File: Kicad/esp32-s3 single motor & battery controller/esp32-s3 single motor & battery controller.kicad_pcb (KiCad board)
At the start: 4 copper layers, 44.9 x 42 mm, 132 parts, among them J1 JST SH SM04B, J2 7 pin FPC 0.3mm, J3 Conn_01x03, J4 Conn_01x03, J5 Batt Balance connector, Q1 NMOS,12v, Q2 NMOS, 12v, Q3 NMOS,12v,PPak, Q4 NMOS, 12v, Q5 NMOS, 12v, Q7 NMOS,12v,PPak, SW1 SW_Push, SW2 SW_Push, U2 AP63203WU, U3 BQ76905RGRR, U4 BQ24780SRUYR, U5 ESP32-S3, U6 74HC595, Y1 40mhz, 10ppm

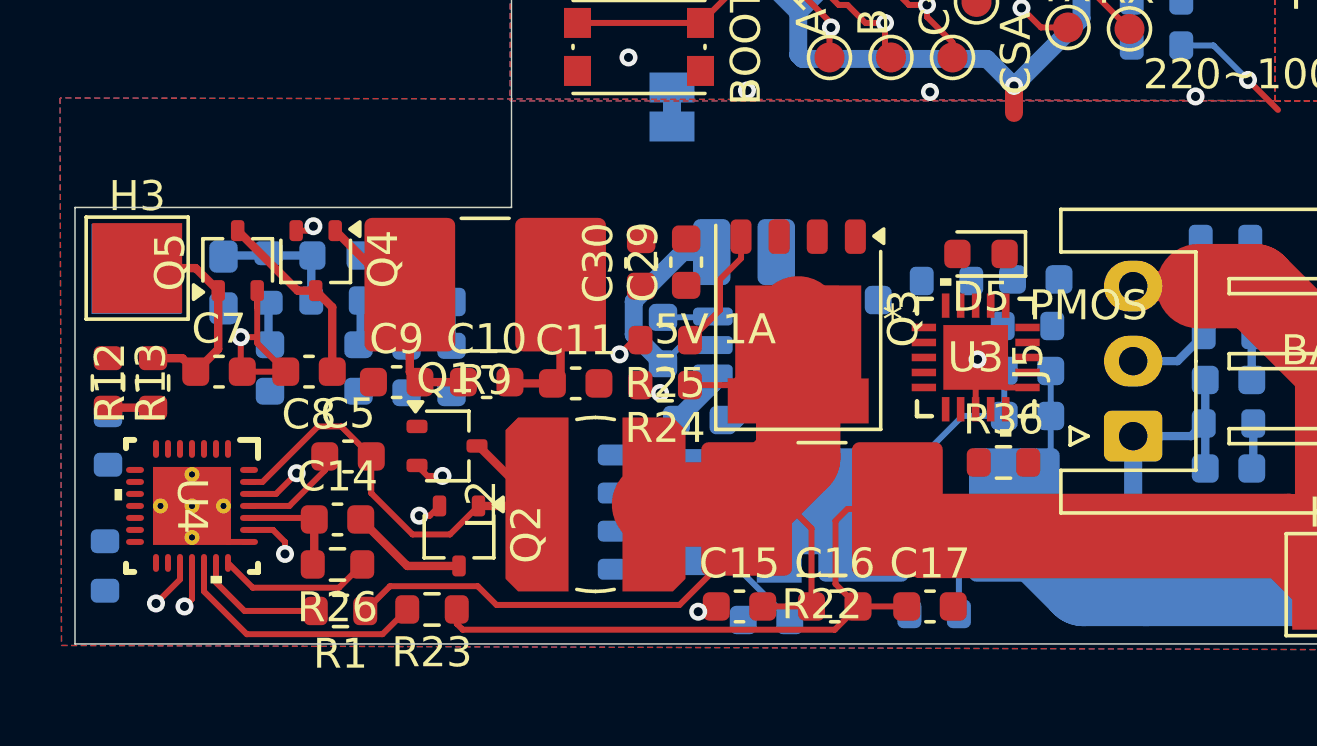
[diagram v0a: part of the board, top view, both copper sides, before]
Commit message: Almost complete charger section, working on balancer
I have a problem with the current sense lines on the balance charger. One loops around with filter capacitors, while the other zigs and zags back and forth on multiple layers! They have to cross each other, and this may lead to a lot of noise.
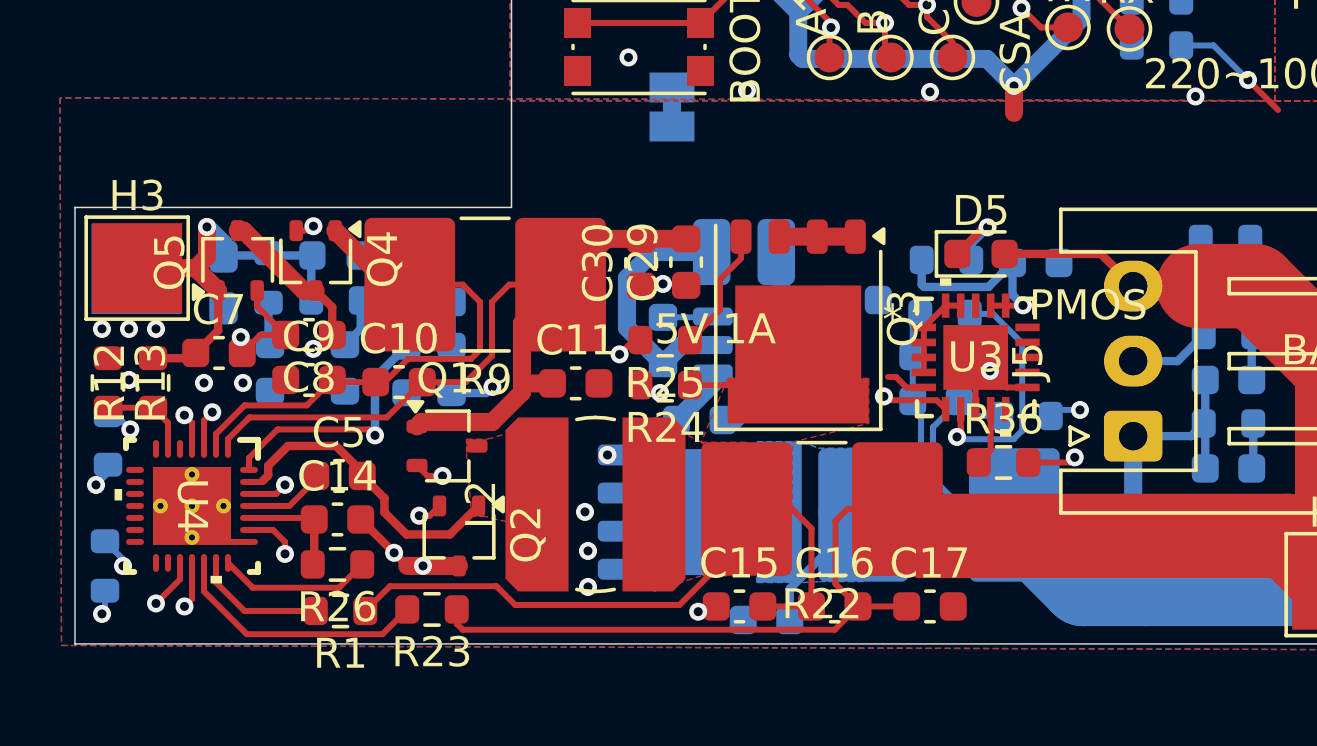
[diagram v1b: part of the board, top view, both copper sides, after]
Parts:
- C11: value 0.01uF -> 0.1uF
- moved R29 7.28 mm to (139.8, 124.4), turned to 180 degrees
- moved C32 3.09 mm to (136.8, 123.9)
- moved C33 3.09 mm to (136.8, 122.4)
- moved C9 2.92 mm to (115.9, 123.2)
- moved C10 2.92 mm to (118.9, 123.3)
- moved R30 2.78 mm to (137.1, 121.0)
- moved C8 1.22 mm to (115.9, 121.7)
- moved C5 0.72 mm to (116.9, 126.4)
- moved R31 0.70 mm to (137.2, 119.2)
- moved C7 0.62 mm to (112.9, 122.3)
- moved C35 0.55 mm to (140.1, 119.3)
- moved C31 0.45 mm to (117.1, 122.8)
- turned D5 to 0 degrees
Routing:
- net /PSU/BATT+: track 59.9 -> 88.8 mm, vias 0 -> 1
- net /MOTORPWR: track 13.5 -> 39.8 mm
- net Net-(Q7-G): track 0.00 -> 17.6 mm, vias 0 -> 2
- net Net-(Q4-S): track 6.36 -> 19.1 mm, vias 0 -> 2
- net Net-(Q3-S): track 36.6 -> 26.4 mm
- net Net-(U3-SRP): track 0.00 -> 10.1 mm, vias 0 -> 2
- net Net-(Q4-D): track 8.07 -> 17.9 mm
- net Net-(U4-CMSRC): track 0.00 -> 8.93 mm, vias 0 -> 2
- net Net-(U4-VCC): track 1.51 -> 9.99 mm, vias 0 -> 1
- net Net-(U3-SRN): track 0.00 -> 8.37 mm, vias 0 -> 1
- net Net-(U3-BAT): track 0.00 -> 6.85 mm, vias 0 -> 1
- net Net-(Q7-S): track 19.6 -> 13.2 mm
- net Net-(U4-ACDRV): track 0.00 -> 5.98 mm, vias 0 -> 2
- net Net-(Q1-S): track 15.8 -> 10.7 mm
- net Net-(Q4-G): track 11.6 -> 14.8 mm, vias 2 -> 3
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- added copper zone on F.Cu, net Net-(Q1-S)
- added copper zone on F.Cu, net Net-(Q3-S)
- added copper zone on B.Cu, net Net-(Q7-S)

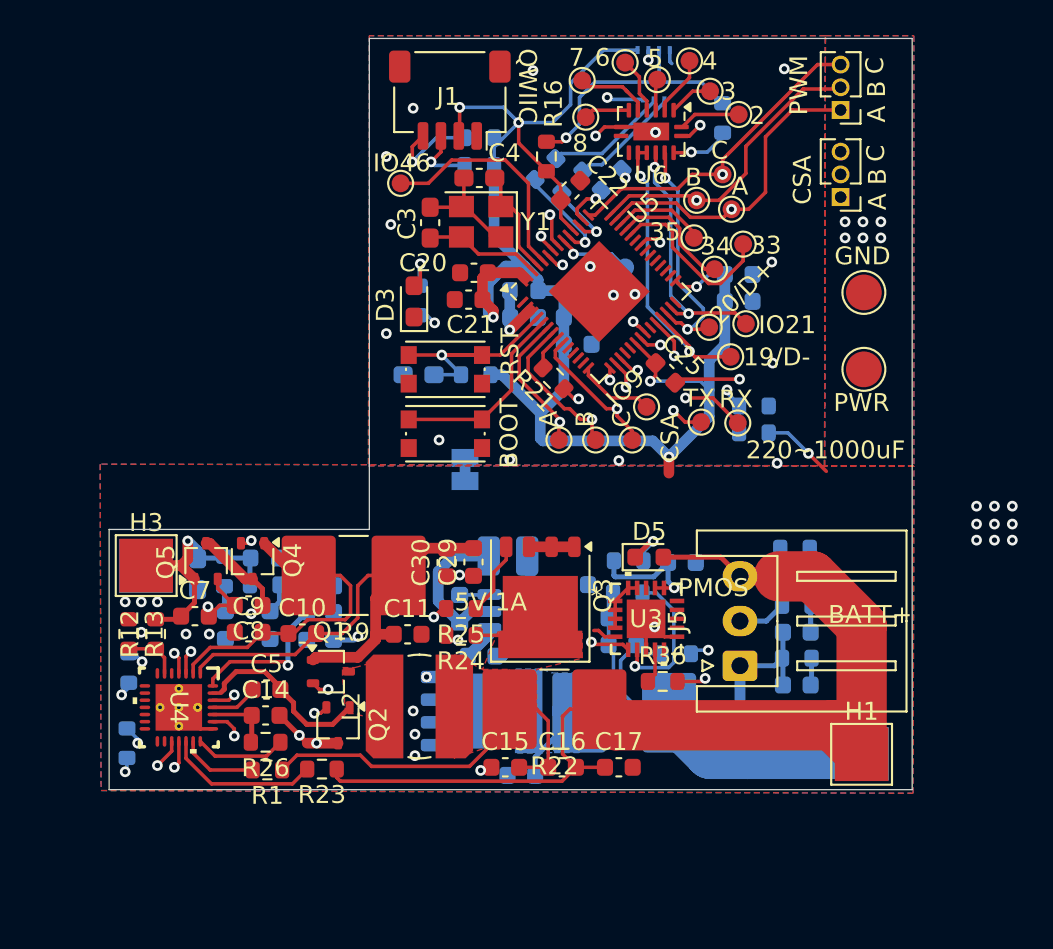
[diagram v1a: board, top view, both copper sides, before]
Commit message: Wiring complete except for i2c
This is the trickiest to wire.
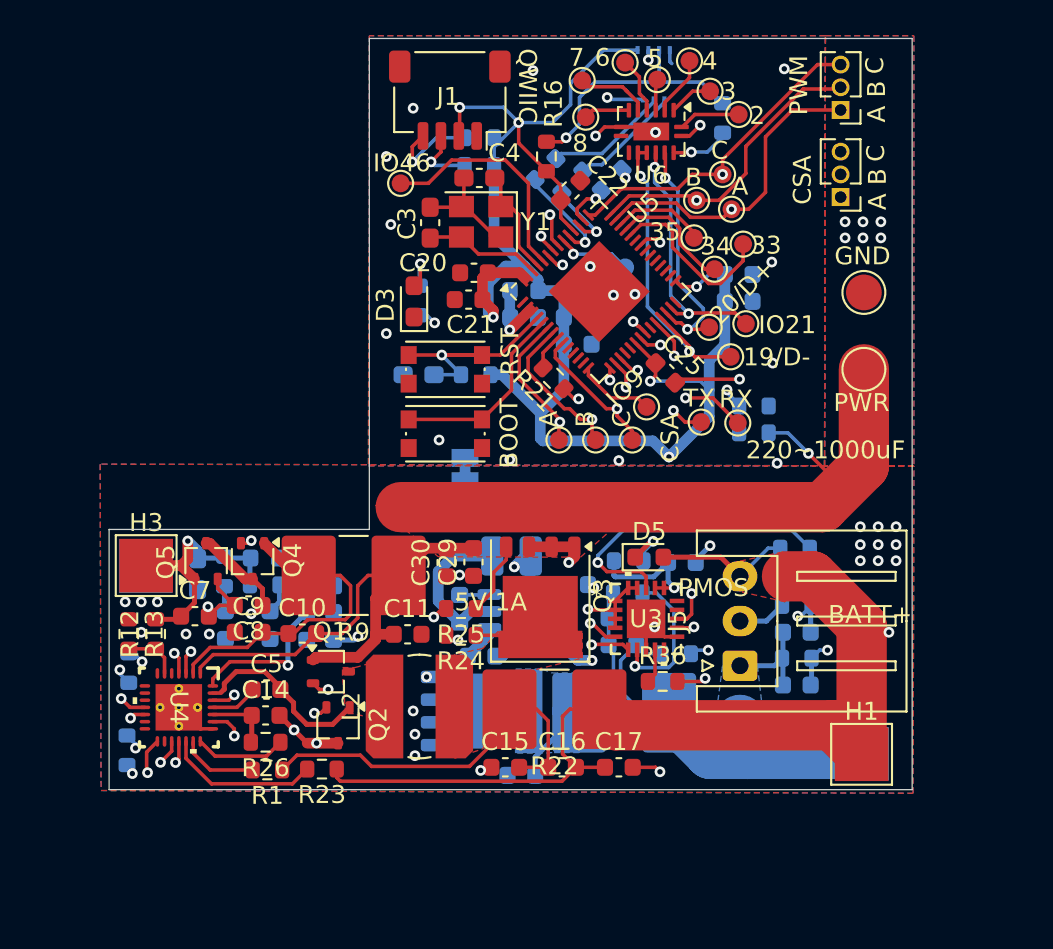
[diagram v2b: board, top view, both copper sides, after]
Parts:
- moved R7 0.40 mm to (109.1, 129.8)
- moved L3 0.20 mm to (130.6, 118.9)
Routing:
- net /PSU/Low: track 2.86 -> 49.1 mm, vias 0 -> 3
- net /MOTORPWR: track 39.8 -> 82.0 mm, vias 1 -> 3
- net /PSU/Up: track 1.52 -> 18.4 mm, vias 0 -> 1
- net /PSU/mid: track 6.91 -> 22.1 mm, vias 0 -> 2
- net VDD: track 103.1 -> 115.6 mm, vias 7 -> 8
- net GND: track 15.8 -> 24.2 mm, vias 20 -> 21
- net Net-(U4-BATDRV): track 24.6 -> 20.8 mm
- net /SDA1: track 21.8 -> 25.4 mm, vias 2 -> 4
- net /PSU/BATT-: track 31.6 -> 28.6 mm
- net GNDPWR: track 12.9 -> 15.8 mm, vias 29 -> 31
- net /PSU/BATT+: track 88.8 -> 90.9 mm, vias 1 -> 2
- net /SCL1: track 25.4 -> 27.2 mm, vias 2 -> 4
- added copper zone on F.Cu, net /MOTORPWR
- added copper zone on F.Cu, net /PSU/BATT+
- added copper zone on B.Cu, net /PSU/BATT-

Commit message: Finished routing
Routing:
- net /SCL1: track 27.2 -> 81.1 mm, vias 4 -> 5
- net /SDA1: track 25.4 -> 77.9 mm, vias 4 -> 5
- net VDD: track 115.6 -> 109.0 mm, vias 8 -> 7
- net Net-(Q4-S): track 18.8 -> 17.7 mm
- net /PSU/Low: track 49.1 -> 50.2 mm
- net Net-(U4-BATSRC): track 22.2 -> 23.1 mm
- net GND: track 24.2 -> 24.1 mm, vias 21 -> 20

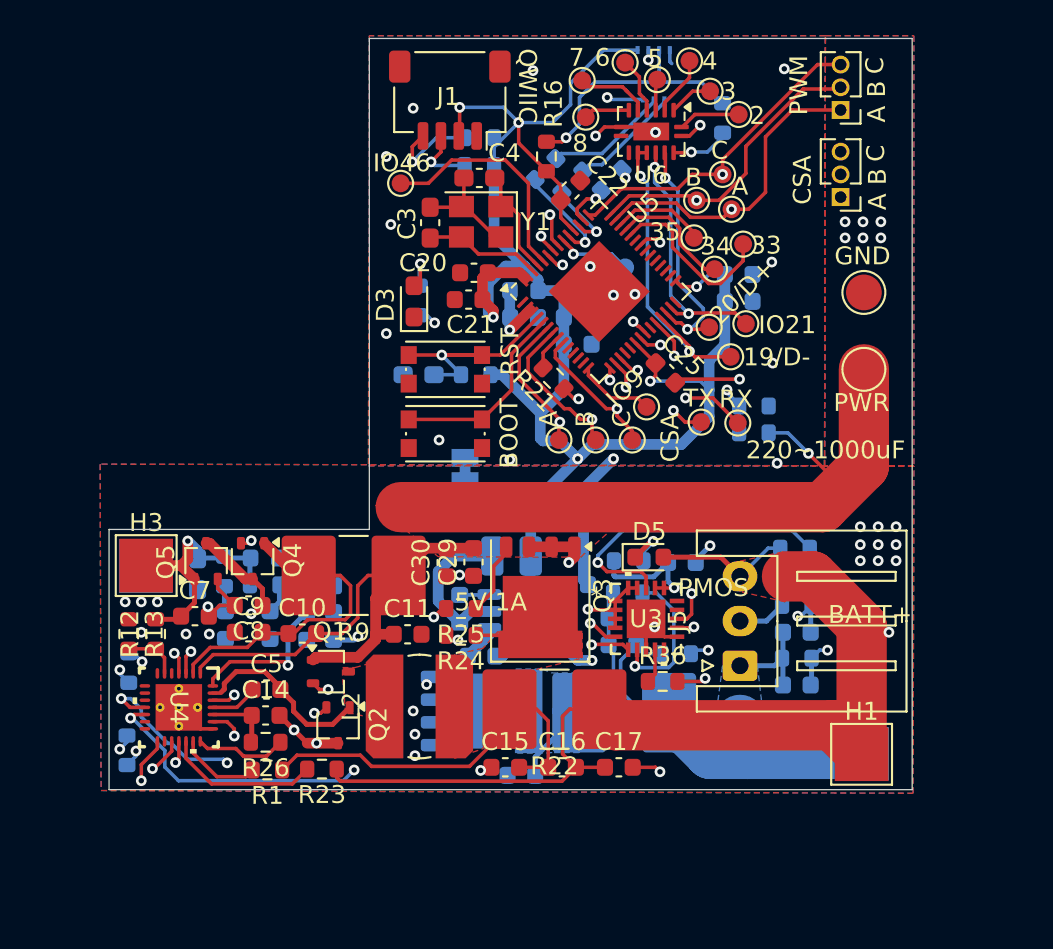
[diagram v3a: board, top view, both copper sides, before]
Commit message: Running DRC and fixing footprints
I had to fix the footprints of the driver chip and the shift register, because there were some undefined pads and the vias were too small.
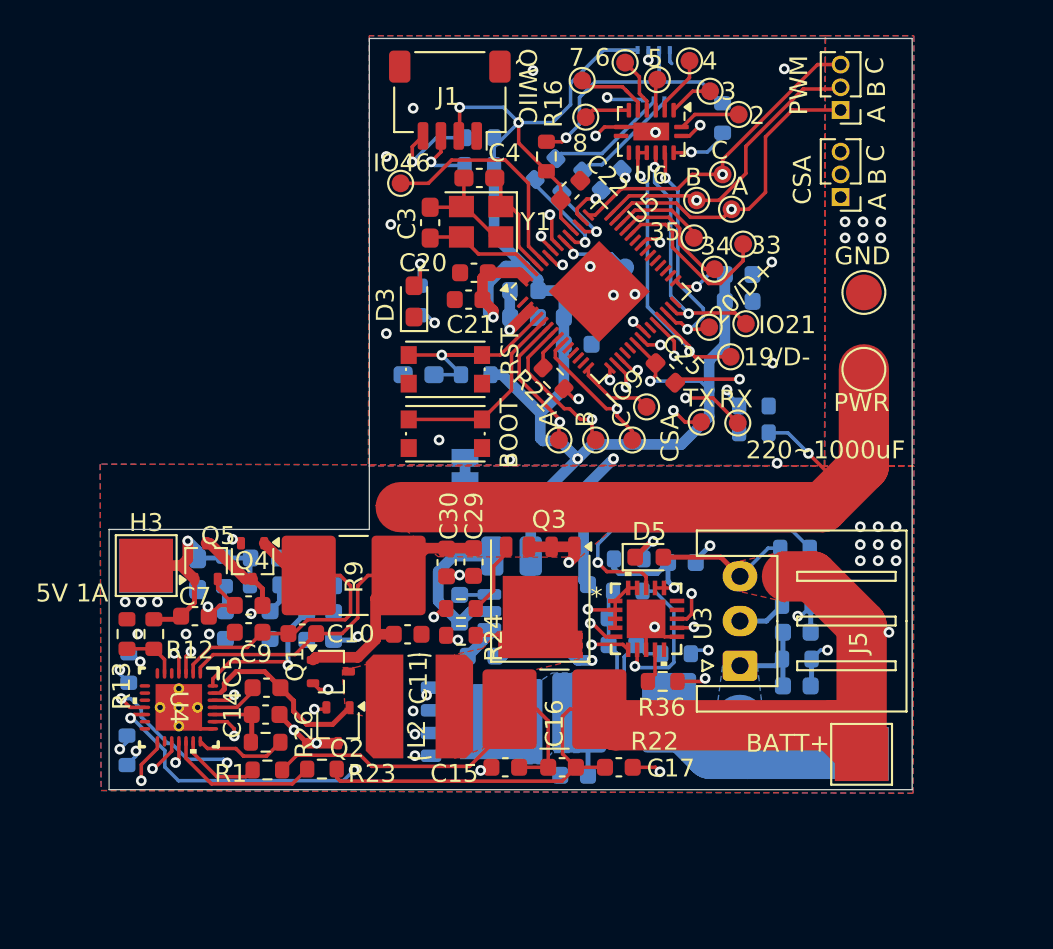
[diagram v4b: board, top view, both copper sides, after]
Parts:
- moved C38 2.95 mm to (134.1, 131.2)
- moved Q7 0.59 mm to (128.8, 128.2)
- moved C5 0.10 mm to (116.9, 126.3)
- moved R12 0.10 mm to (110.6, 123.3)
- moved R13 0.10 mm to (109.1, 123.3)
- moved R31 0.10 mm to (137.2, 119.1)
- moved R30 0.10 mm to (137.1, 120.9)
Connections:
- U6 pad 17: (no net) -> GND
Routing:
- net GND: track 24.1 -> 24.7 mm
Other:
- board text removed: "PMOS"

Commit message: Finished PCB with 2s battery charger
Silkscreen is all finished
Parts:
- added C41: 220uF, Capacitor_SMD:CP_Elec_6.3x9.9, F.Cu at (147.8, 111.3)
- moved H6 3.70 mm to (150.3, 104.8)
- moved H5 2.30 mm to (150.3, 101.9)
- moved C35 0.30 mm to (140.1, 119.0)
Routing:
- net GNDPWR: track 15.9 -> 23.3 mm
- net /MOTORPWR: track 82.0 -> 85.7 mm
- net VDD: track 109.0 -> 108.8 mm, vias 7 -> 6
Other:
- outline, holes or cut-outs redrawn
- board text added: "220uF"
- board text added: "⊕"
- board text added: "⊖"
- board text removed: "220~1000uF"
- board text removed: "5V 1A"
- board text removed: "GNDPWR"

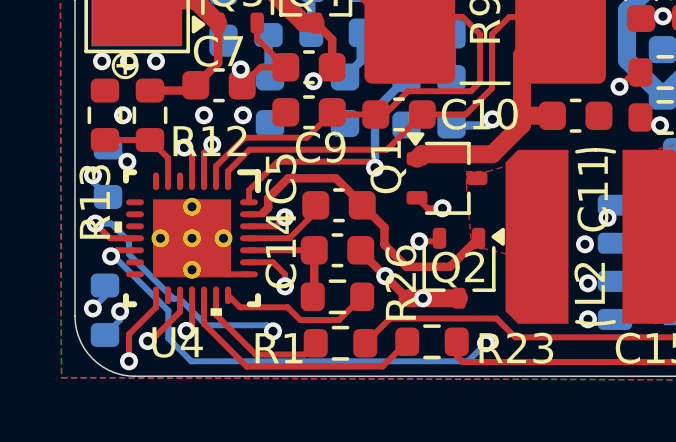
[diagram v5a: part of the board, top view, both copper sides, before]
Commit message: Removed battery voltage divider, fixed BATTPres indicator
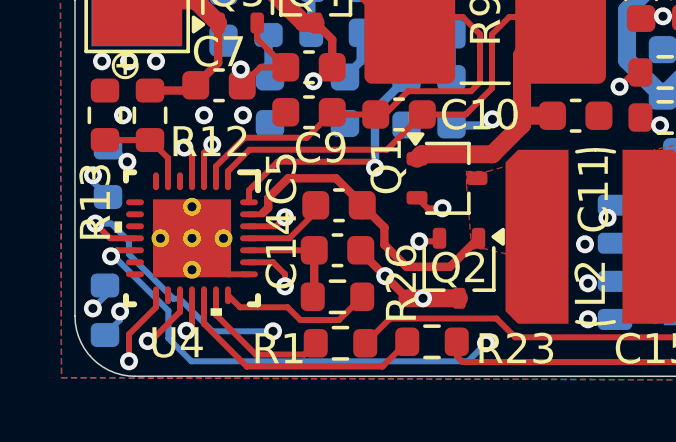
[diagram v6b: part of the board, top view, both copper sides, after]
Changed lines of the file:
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@@
 		(tags "test point SMD pad rectangle square")
 		(property "Reference" "H4"
-			(at -2.5 -1.25 270)
+			(at -2.5 -1.25 -90)
 			(layer "B.SilkS")
 			(hide yes)
@@
 	)
 	(segment
-		(start 109.9 127.5)
-		(end 109.309517 126.909517)
+		(start 111.591308 129.413769)
+		(end 111.379454 129.413769)
 		(width 0.2)
 		(layer "B.Cu")
@@
 	)
 	(segment
-		(start 111.379454 129.413769)
-		(end 109.9 127.934314)
+		(start 109.9 127.5)
+		(end 109.309517 126.909517)
 		(width 0.2)
 		(layer "B.Cu")
@@
 	(segment
 		(start 114.7 130.5)
-		(end 114.5 130.3)
+		(end 112.677539 130.5)
 		(width 0.2)
 		(layer "B.Cu")
@@
 	)
 	(segment
-		(start 112.477539 130.3)
+		(start 112.677539 130.5)
 		(end 111.591308 129.413769)
 		(width 0.2)
@@
 	)
 	(segment
-		(start 126.1 96.9)
-		(end 126.3 97.1)
-		(width 0.2)
-		(layer "B.Cu")
-		(net 21)
-	)
-	(segment
 		(start 109.309517 126.909517)
 		(end 108.778216 126.909517)
@@
 	)
 	(segment
-		(start 114.5 130.3)
-		(end 112.477539 130.3)
+		(start 126.1 96.9)
+		(end 126.3 97.1)
 		(width 0.2)
 		(layer "B.Cu")
@@
 	)
 	(segment
-		(start 111.591308 129.413769)
-		(end 111.379454 129.413769)
+		(start 111.379454 129.413769)
+		(end 109.9 127.934314)
 		(width 0.2)
 		(layer "B.Cu")
